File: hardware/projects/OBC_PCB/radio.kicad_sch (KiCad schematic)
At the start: 11 parts, among them J7 RF coax pads

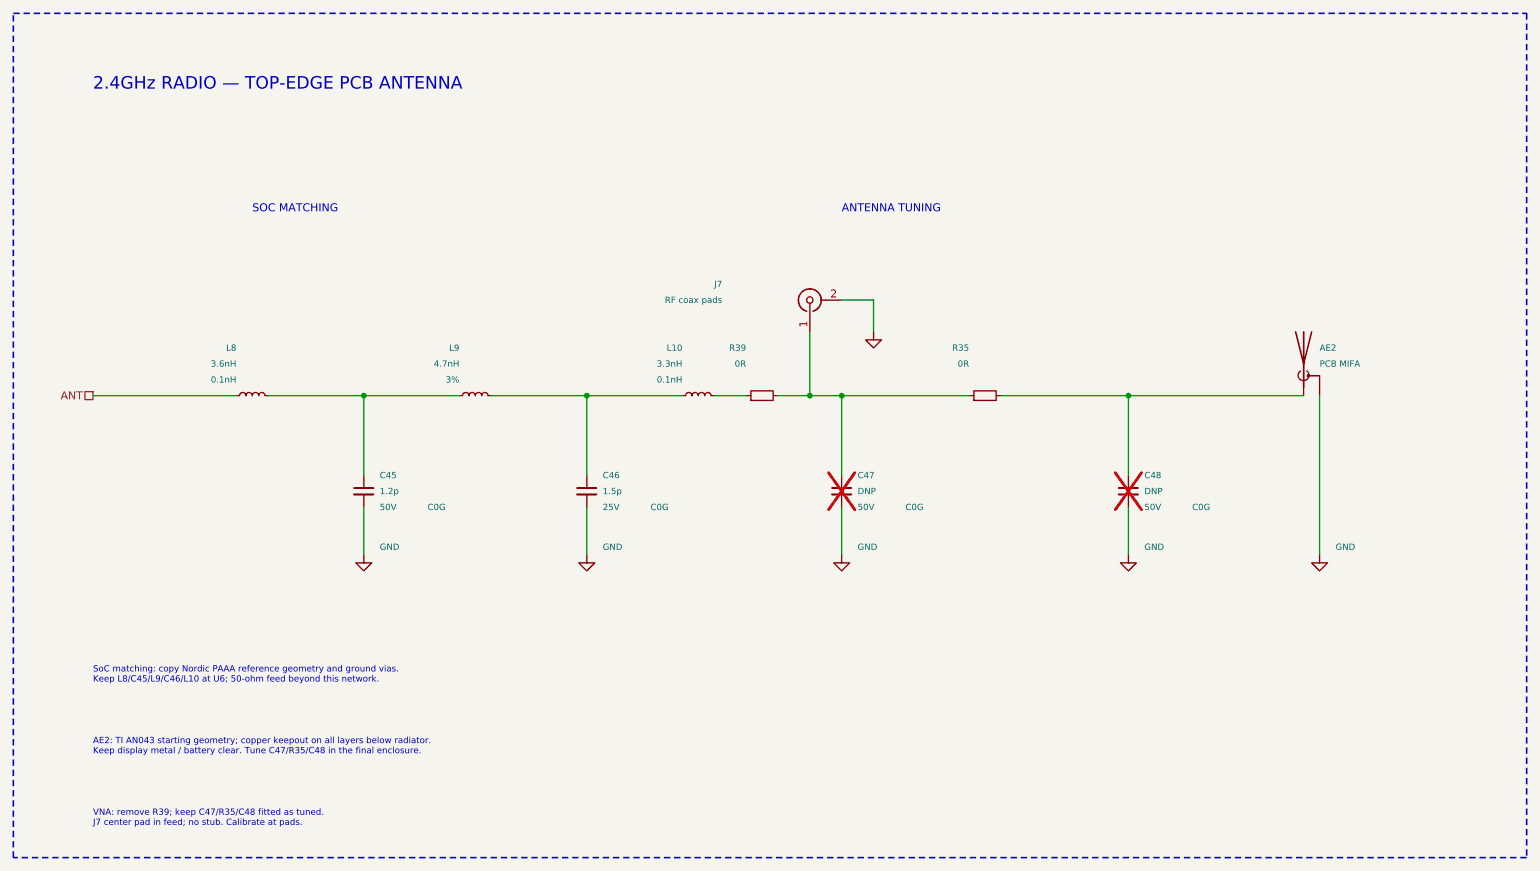
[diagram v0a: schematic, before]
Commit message: fix(hardware): apply schematic review and peripheral pin mapping
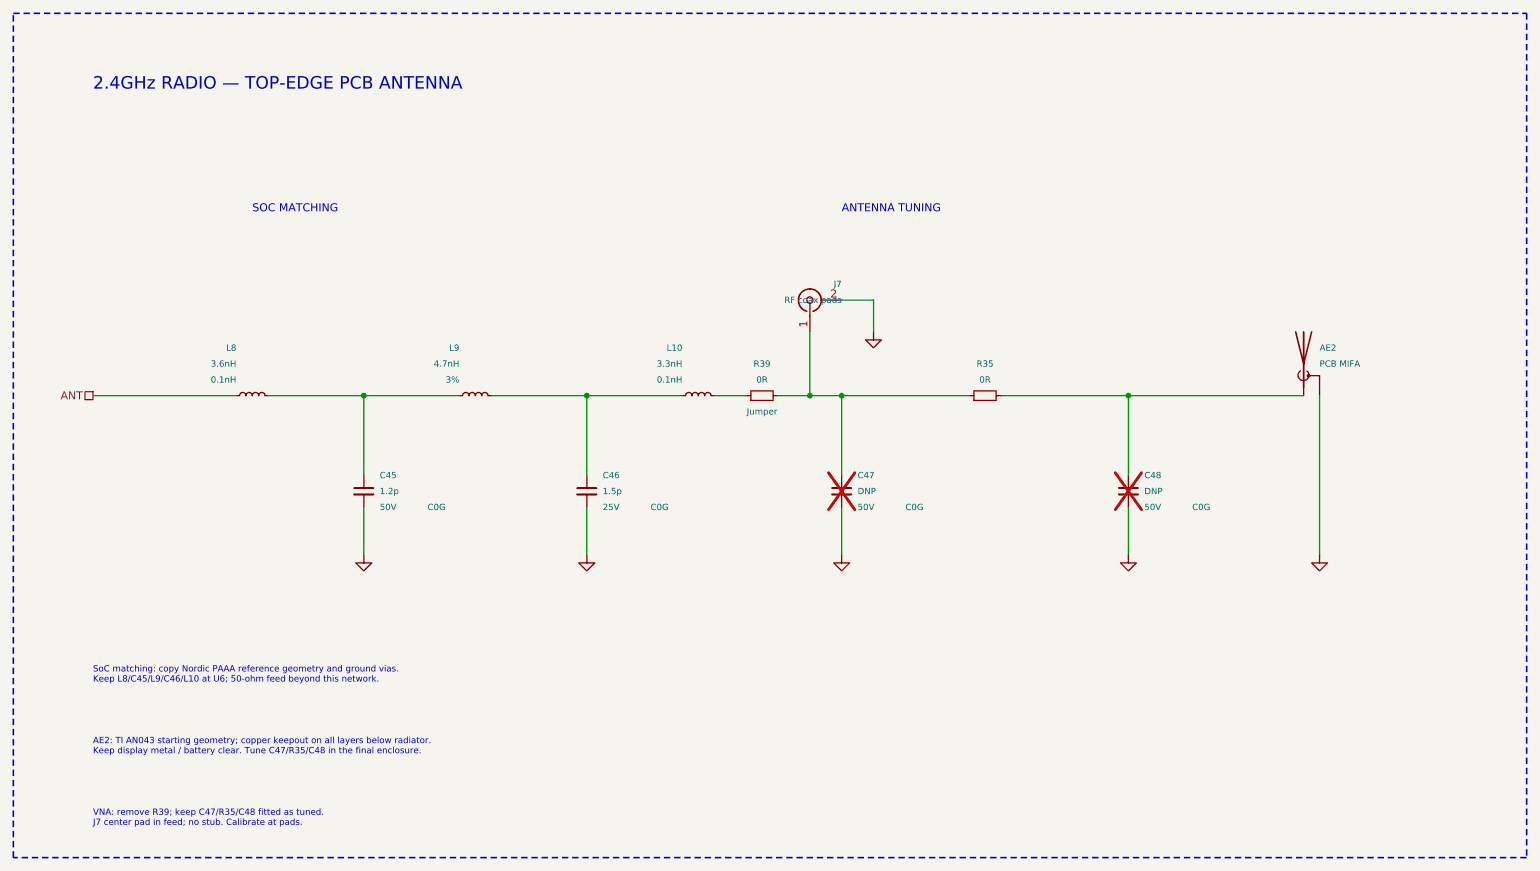
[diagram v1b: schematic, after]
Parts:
- C45, C46: footprint Capacitor_SMD:C_0201_0603Metric -> obc:C_Nordic_0201_0603Metric
- L10, L8, L9: footprint Inductor_SMD:L_0201_0603Metric -> obc:L_Nordic_0201_0603Metric

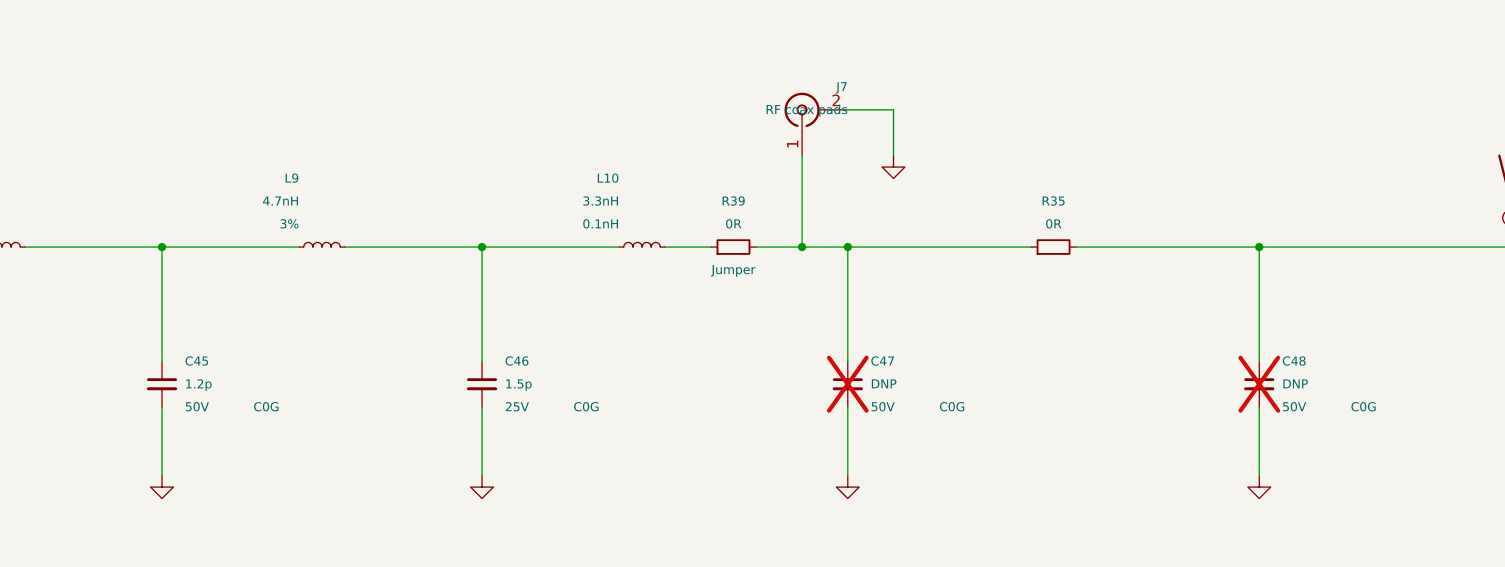
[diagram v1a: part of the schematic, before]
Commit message: hardware: name critical nets and ground connector tabs
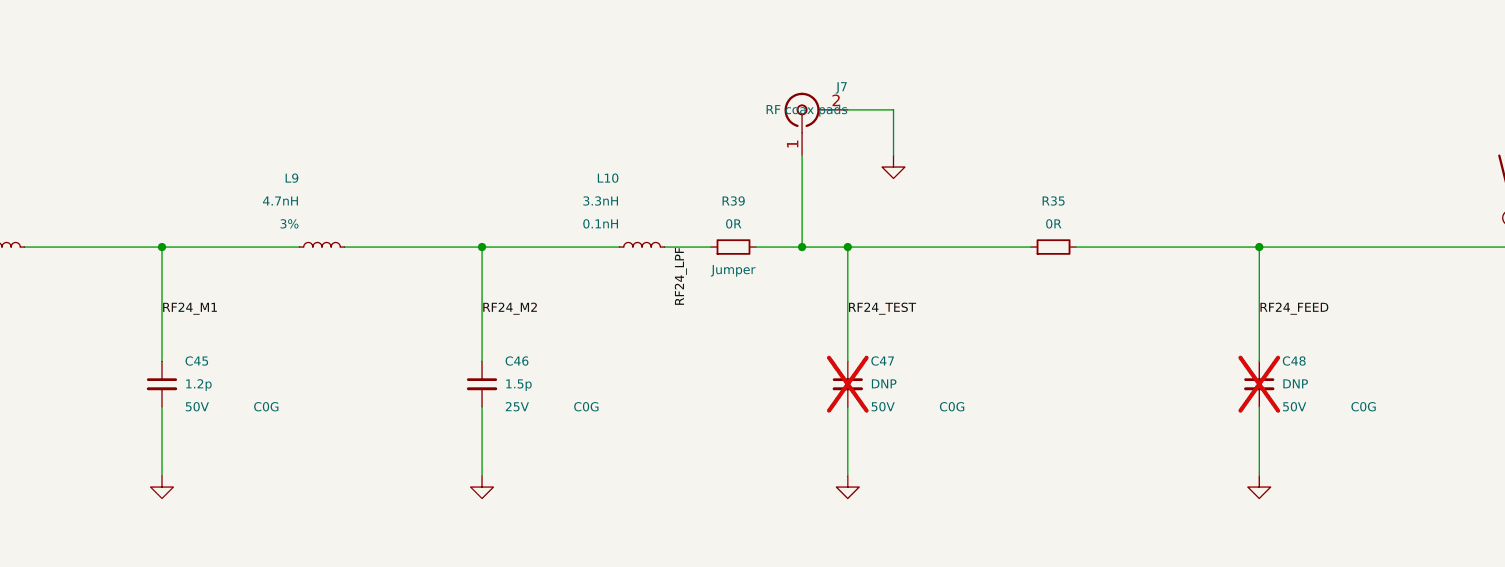
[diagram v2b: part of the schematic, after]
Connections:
- net RF24_M2: now reaches C46.1, L10.1, L9.2
- net RF24_FEED: now reaches AE2.1 (FEED), C48.1, R35.2
- net RF24_TEST: now reaches C47.1, J7.1 (In), R35.1, R39.2
- net RF24_M1: now reaches C45.1, L8.2, L9.1
- net RF24_LPF: now reaches L10.2, R39.1

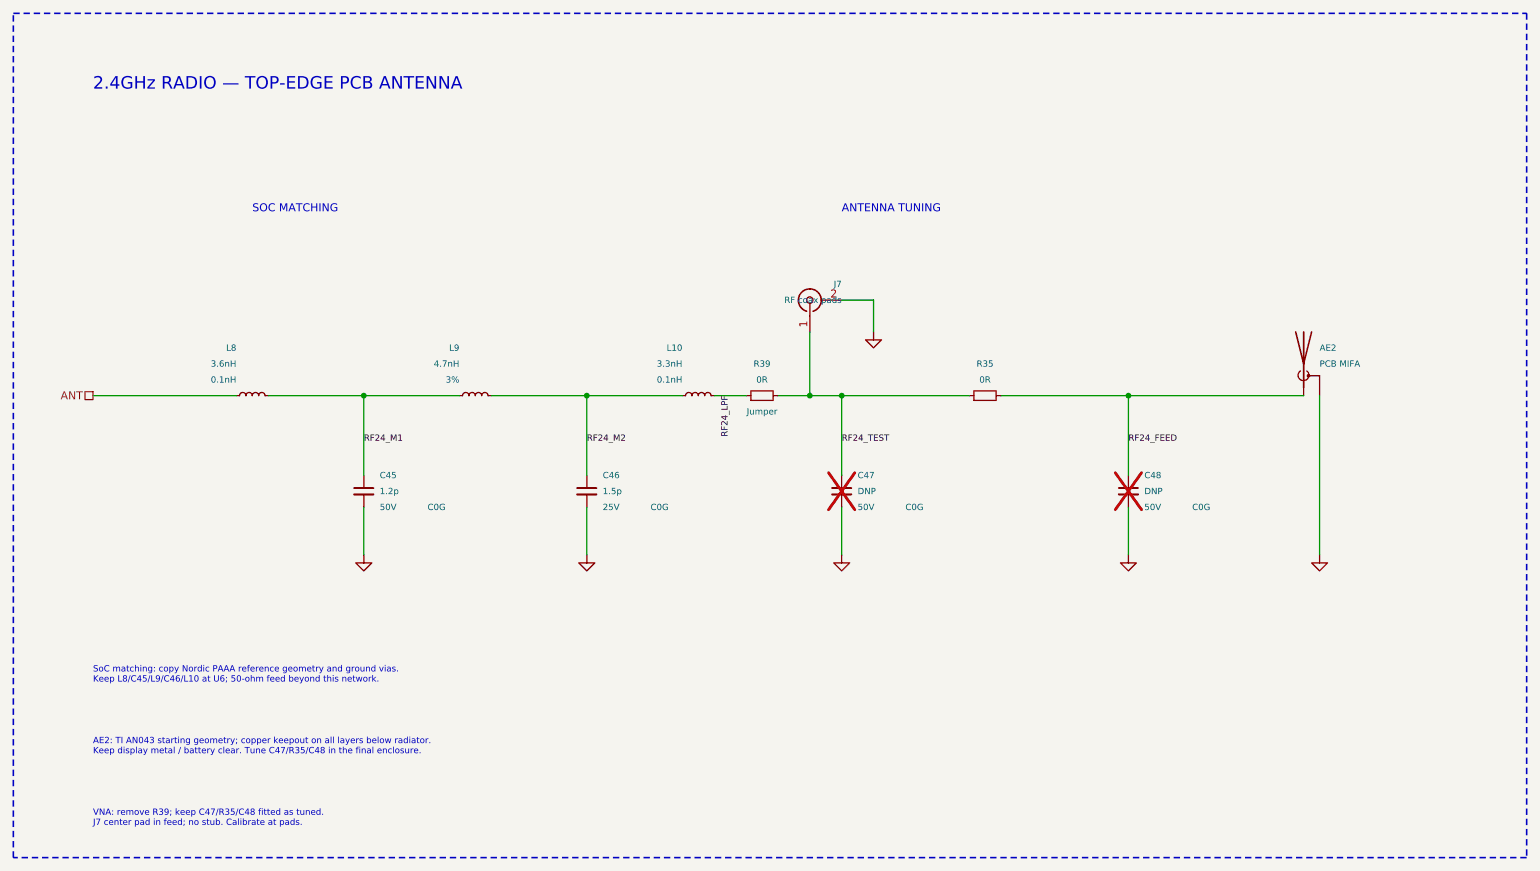
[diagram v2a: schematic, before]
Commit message: hardware: prepare QFN schematic for non-HDI boards
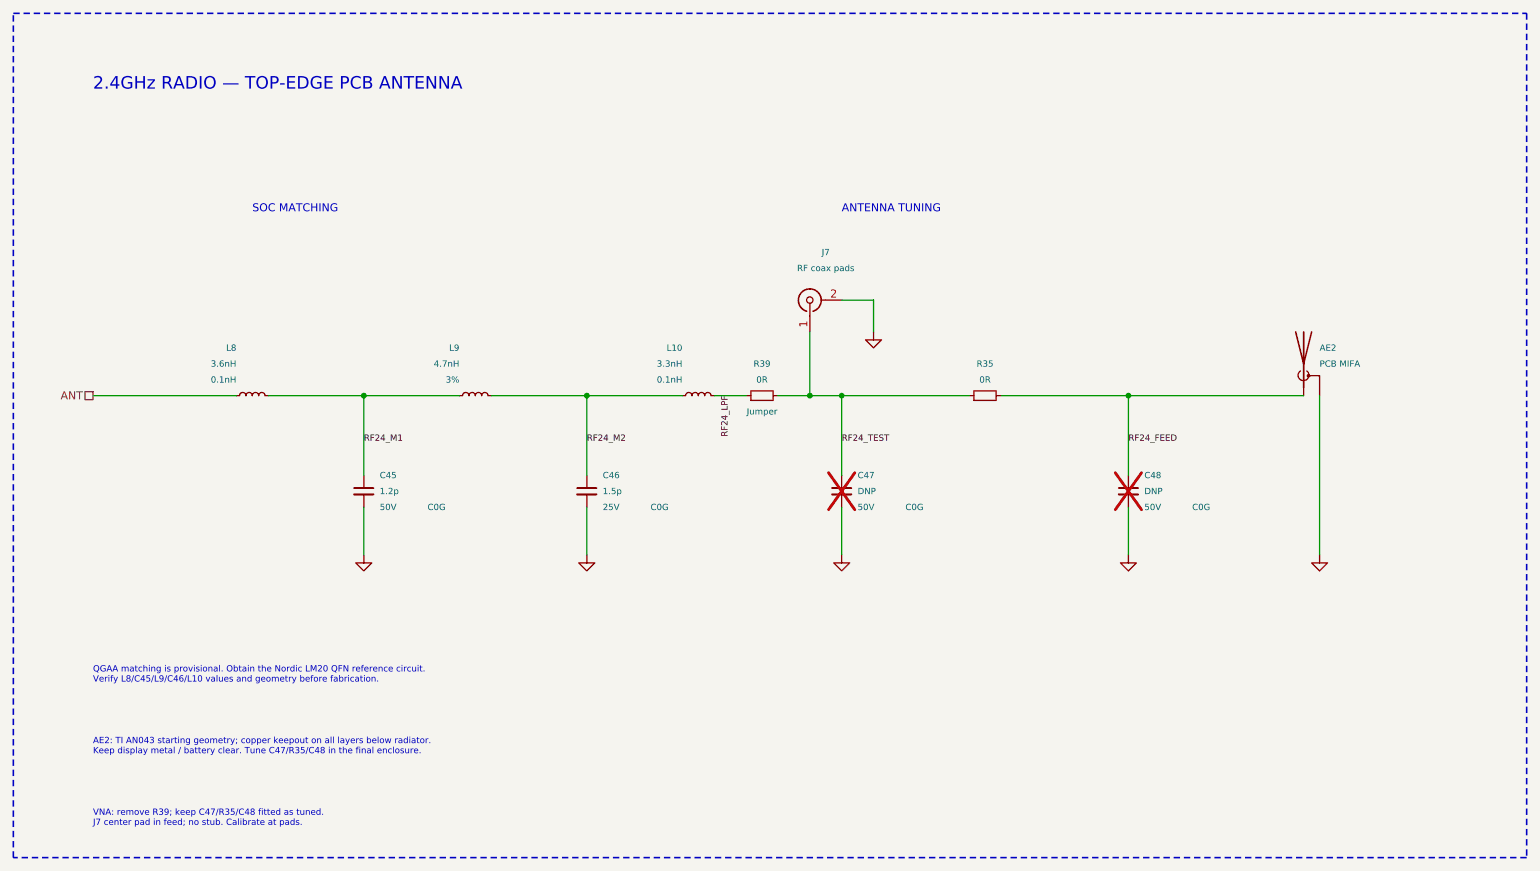
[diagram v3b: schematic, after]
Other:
- note added: "QGAA matching is provisional. Obtain the Nordic LM20 QFN reference circuit. Verify L8/C45/L9/C46/L10 values and geometry before fabrication."
- note removed: "SoC matching: copy Nordic PAAA reference geometry and ground vias. Keep L8/C45/L9/C46/L10 at U6; 50-ohm feed beyond this network."
